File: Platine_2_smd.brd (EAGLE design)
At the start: 88.9 x 101.6 mm, 21 parts, among them X2 DTF13-12PA

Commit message: Updated Libraries !
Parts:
- BLINKER_LINKS, BLINKER_RECHTS: value Gelb -> 156120SS82500
- BREMSLEUCHTE, LICHT_LINKS, LICHT_RECHTS: value Rot -> 156120SS82500
- LADELEITUNG, NEBELSCHLUSSLEUCHTE, RUECKFAHRLEUCHTE, STROMVERSORGUNG: value Grün -> 156120SS82500

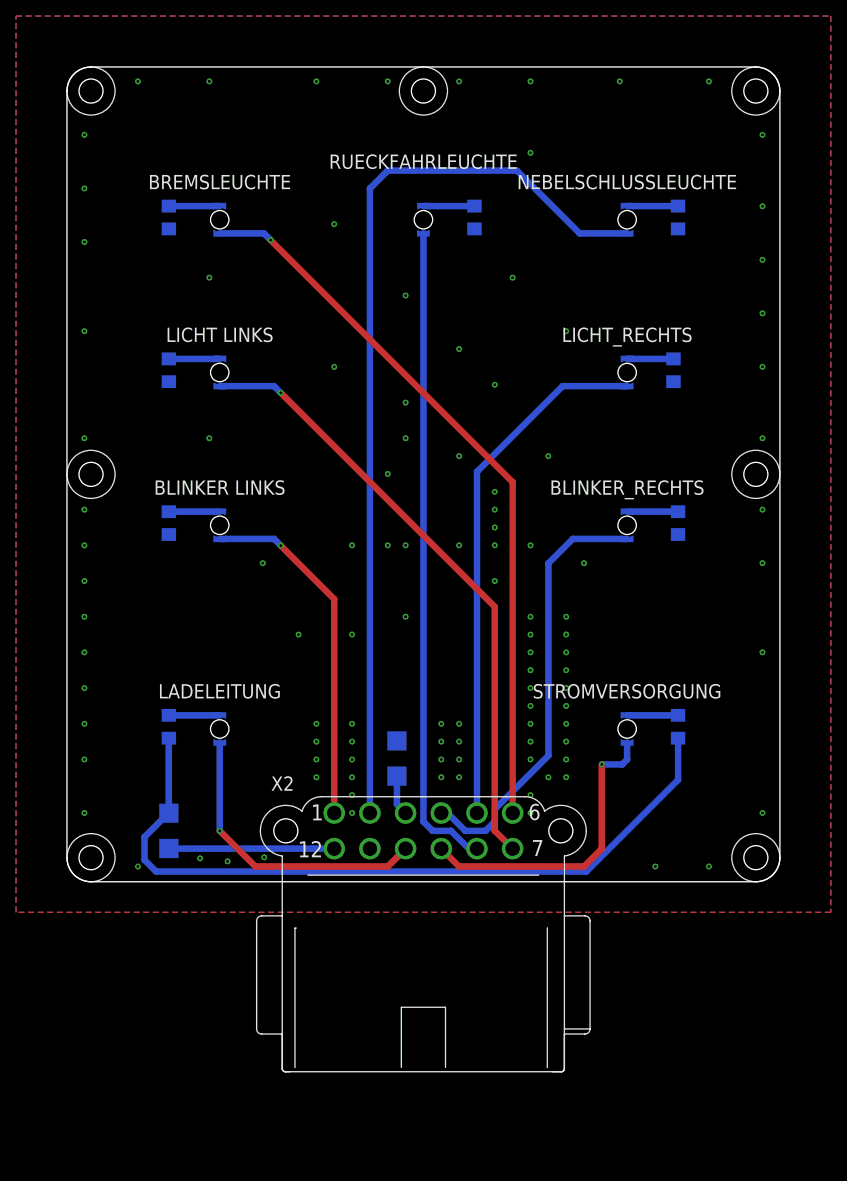
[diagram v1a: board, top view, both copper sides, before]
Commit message: Farben der LEDS
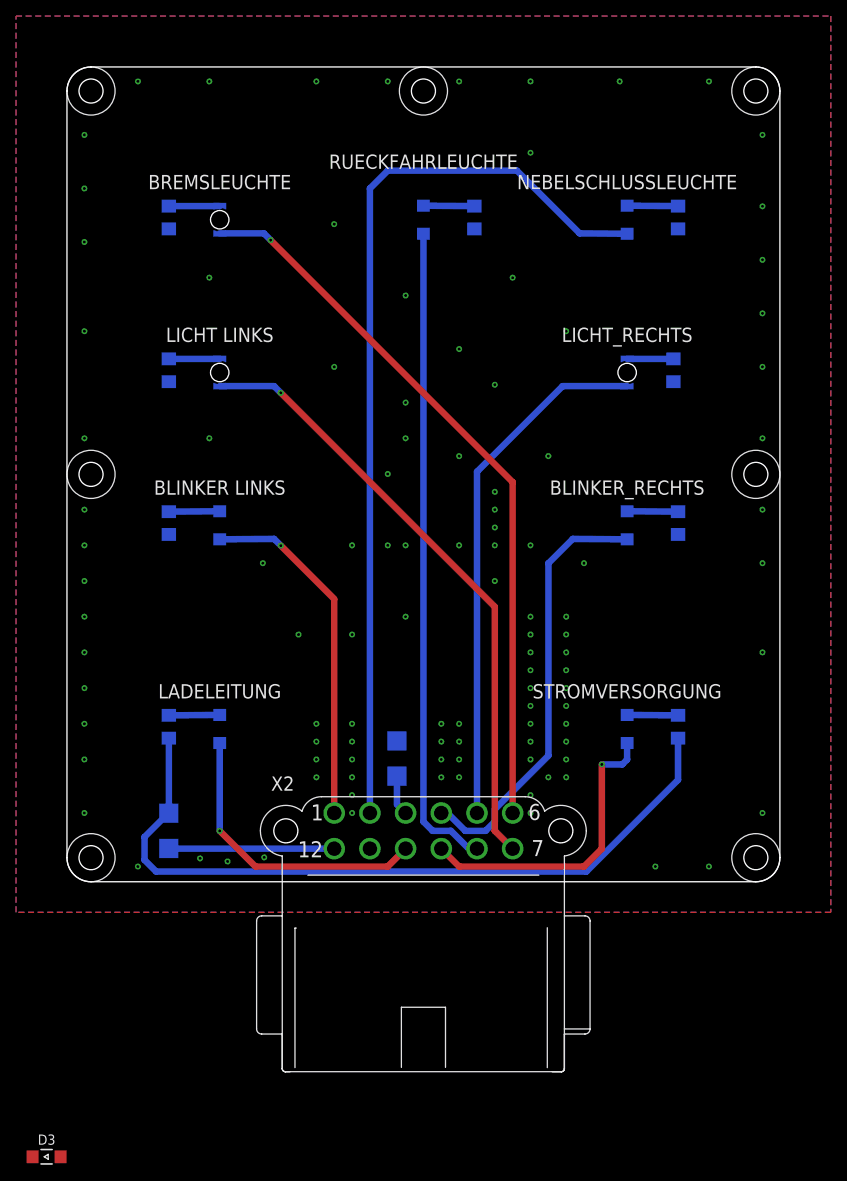
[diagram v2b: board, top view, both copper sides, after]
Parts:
- added D3: 156120VS82500, Wurth_LEDs_WL-SMRW:WL-SMRW_1206_DOME
- BLINKER_LINKS, BLINKER_RECHTS: value 156120SS82500 -> 156120YS82500; device Wurth_LEDs_WL-SMRW:WL-SMRW_1206_DOME_REV -> Wurth_LEDs_WL-SMRW:WL-SMRW_1206_DOME
- LADELEITUNG, NEBELSCHLUSSLEUCHTE, RUECKFAHRLEUCHTE, STROMVERSORGUNG: value 156120SS82500 -> 156120VS82500; device Wurth_LEDs_WL-SMRW:WL-SMRW_1206_DOME_REV -> Wurth_LEDs_WL-SMRW:WL-SMRW_1206_DOME

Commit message: ..
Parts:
- removed D3: 156120VS82500, Wurth_LEDs_WL-SMRW:WL-SMRW_1206_DOME
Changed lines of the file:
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@@
 <attribute name="VALUE" x="-6.731" y="6.858" size="1.27" layer="28" rot="MR90"/>
-</element>
-<element name="D3" library="Wurth_LEDs_WL-SMRW" library_urn="urn:adsk.eagle:library:19040144" package="WL-SMRW_1206_DOME" package3d_urn="urn:adsk.eagle:package:19040155/3" value="156120VS82500" x="-46.99" y="-40.64" smashed="yes">
-<attribute name="CHIP-TECHNOLOGY" value="AlInGaP" x="-46.99" y="-40.64" size="1.778" layer="27" display="off"/>
-<attribute name="DATASHEET-URL" value="https://www.we-online.com/redexpert/spec/156120VS82500?ae" x="-46.99" y="-40.64" size="1.778" layer="27" display="off"/>
-<attribute name="DOMINANT-WAVELENGTH" value="573nm" x="-46.99" y="-40.64" size="1.778" layer="27" display="off"/>
-<attribute name="EMITTING-COLOR" value="Bright Green" x="-46.99" y="-40.64" size="1.778" layer="27" display="off"/>
-<attribute name="FORWARD-VOLTAGE" value="2V" x="-46.99" y="-40.64" size="1.778" layer="27" display="off"/>
-<attribute name="LUMINOUS-INTENSITY" value="1050mcd" x="-46.99" y="-40.64" size="1.778" layer="27" display="off"/>
-<attribute name="NAME" x="-46.99" y="-39.14" size="1.27" layer="25" align="bottom-center"/>
-<attribute name="PART-NUMBER" value="156120VS82500" x="-46.99" y="-40.64" size="1.778" layer="27" display="off"/>
-<attribute name="PEAK-WAVELENGTH" value="575nm" x="-46.99" y="-40.64" size="1.778" layer="27" display="off"/>
-<attribute name="VALUE" x="-46.99" y="-43.34" size="1.27" layer="27" align="bottom-center"/>
-<attribute name="VIEWING-ANGLE" value="20°" x="-46.99" y="-40.64" size="1.778" layer="27" display="off"/>
 </element>
 </elements>
